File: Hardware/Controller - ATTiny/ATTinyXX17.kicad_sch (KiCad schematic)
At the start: 37 parts, among them U1 ATtiny1617

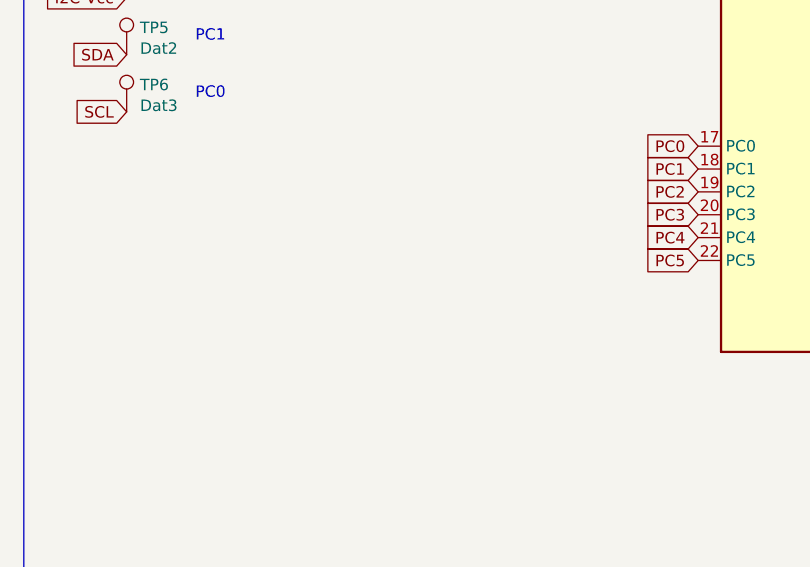
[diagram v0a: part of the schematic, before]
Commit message: Added a reset button to ATTiny controller board
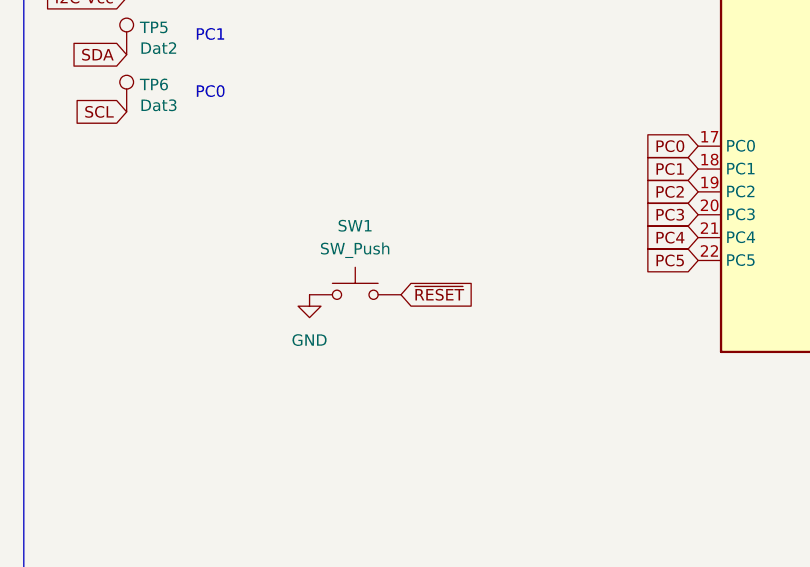
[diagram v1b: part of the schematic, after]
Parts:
- added SW1: SW_Push, tinker:SW_Push_TS273014TP, symbol Switch:SW_Push
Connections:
- net GND: now also SW1.1
- net ~{RESET}: now also SW1.2
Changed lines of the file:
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@@
+    )
+  )
+  (global_label "~{RESET}" (shape input) (at 69.85 123.19 0) (fields_autoplaced)
+    (effects (font (size 1.27 1.27)) (justify left))
+    (property "Intersheet References" "${INTERSHEET_REFS}" (id 0) (at 77.9194 123.2694 0)
+      (effects (font (size 1.27 1.27)) (justify left) hide)
     )
   )
@@
     (pin "1")
   )
+  (symbol (lib_id "power:GND") (at 59.69 123.19 0) (unit 1)
+    (in_bom yes) (on_board yes) (fields_autoplaced)
+    (property "Reference" "#PWR0113" (id 0) (at 59.69 129.54 0)
+      (effects (font (size 1.27 1.27)) hide)
+    )
+    (property "Value" "GND" (id 1) (at 59.69 128.27 0))
+    (property "Footprint" "" (id 2) (at 59.69 123.19 0)
+      (effects (font (size 1.27 1.27)) hide)
+    )
+    (property "Datasheet" "" (id 3) (at 59.69 123.19 0)
+      (effects (font (size 1.27 1.27)) hide)
+    )
+    (pin "1")
+  )
   (symbol (lib_id "Connector:TestPoint") (at 222.25 67.31 0) (unit 1)
     (in_bom no) (on_board yes)
@@
     (pin "1")
   )
+  (symbol (lib_id "Switch:SW_Push") (at 64.77 123.19 0) (unit 1)
+    (in_bom yes) (on_board yes) (fields_autoplaced)
+    (property "Reference" "SW1" (id 0) (at 64.77 115.57 0))
+    (property "Value" "SW_Push" (id 1) (at 64.77 118.11 0))
+    (property "Footprint" "tinker:SW_Push_TS273014TP" (id 2) (at 64.77 118.11 0)
+      (effects (font (size 1.27 1.27)) hide)
+    )
+    (property "Datasheet" "~" (id 3) (at 64.77 118.11 0)
+      (effects (font (size 1.27 1.27)) hide)
+    )
+    (pin "1")
+    (pin "2")
+  )
   (symbol (lib_id "Connector:TestPoint") (at 39.37 96.52 0) (unit 1)
